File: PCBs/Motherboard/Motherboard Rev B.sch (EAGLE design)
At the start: 29 parts, among them Q1 32kHZ, U1 Value, U2 TPS22942DCKR

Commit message: So. many. changes.
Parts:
- removed U2: TPS22942DCKR, TPS22942:TPS22942DCKR
- added C14: 10uF, adafruit:C-USC0805
- added DF11: DF11-8DP-2DS(52), DF11:DF11-8DP-2DS(52)
- added J1: MOLEX_504050-0491, Molex 504050-0491:MOLEX_504050-0491
- added JTAG_PWR: MOLEX_SL_03-87898, molex-sl-connectors_jw:MOLEX_SL_03-87898
- added LTC6081: LTC6081HMS8PBF, LTC6081:LTC6081HMS8PBF
- added R10, R11, R17, R18, R19, R9: 350, resistor:R-US_R0805
- added R12, R20: 50, Bourns 3224J:3224J
- added R13, R14, R21, R22: 10k, resistor:R-US_R0805
- added R15, R16, R23, R24: 330k, resistor:R-US_R0805
- added R6, R8: 100k, resistor:R-US_R0805
- added R7: 0, resistor:R-US_R0805
- added TPS22942: TPS22942DCKR, TPS22942:TPS22942DCKR
- added U$3: FPF2105, FPF2105:FPF2105
- C12: value 2.2nF -> 1nF
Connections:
- removed net INT: U$2.INT
- removed net N$4 (its old number): C18.1, Q1.1, U1.PJ.7_HFXOUT
- removed net RST: C12.1, JTAG-11.KL, R5.1, U1.RST_NMI_SBWTDIO_N
- removed net TCK: JTAG-7.KL, U1.PJ.3_TCK_SRCPUOFF_C9
- removed net TDI: JTAG-3.KL, U1.PJ.1_TDI_TCLK_MCLK_SRSCG0_C7
- removed net TDO: JTAG-1.KL, U1.PJ.0_TDO_TB0OUTH_SMCLK_SRSCG1_C6
- removed net TEST: JTAG-8.KL, U1.TEST_SBWTCK
- removed net TMS: JTAG-5.KL, U1.PJ.2_TMS_ACLK_SROSCOFF_C8
- new net 3V1: C14.1
- new net 3V3_SD: C13.1, C16.1, R1.1, U$11.VDD, U$3.VOUT
- new net EXT_RXD: JTAG-14.KL, U1.P2.6_TB0.1_UCA1RXD_UCA1SOMI
- new net EXT_TXD: JTAG-12.KL, U1.P2.5_TB0.0_UCA1TXD_UCA1SIMO
- new net INT_IMU: U$2.INT, U1.P8.1
- new net N$10: LTC6081.-INA, R14.2, R16.2
- new net N$11: R18.2, R19.1, R21.1
- new net N$12: LTC6081.+INB, R21.2, R23.2
- new net N$13: LTC6081.-INB, R22.2, R24.2
- new net N$2: R6.2, R7.2, U$3.ON
- new net N$6: C18.1, Q1.1, U1.PJ.4_LFXIN
- new net N$7: R8.2, U$3.FLAGB
- new net N$8: R10.2, R11.1, R13.1
- new net N$9: LTC6081.+INA, R13.2, R15.2
- new net SBWTCK: JTAG-7.KL, U1.TEST_SBWTCK
- new net SBWTDIO: C12.1, JTAG-1.KL, R5.1, U1.RST_NMI_SBWTDIO_N
- new net STR1: LTC6081.OUTA, R16.1, U1.P3.1_A13_C13
- new net STR1_L1: DF11.1, R12.WIPER
- new net STR1_L2: DF11.2, R9.2
- new net STR1_L3: DF11.3, R14.1
- new net STR2: LTC6081.OUTB, R24.1, U1.P3.2_A14_C14
- new net STR2_L1: DF11.4, R20.WIPER
- new net STR2_L2: DF11.5, R17.2
- new net STR2_L3: DF11.6, R22.1
- new net SW5: J1.1, U$1.SW5_5V
- new net TMP_L1: DF11.7
- new net TMP_L2: DF11.8
- new net VCC_TARGET: JTAG-4.KL, JTAG_PWR.3
- new net VCC_TOOL: JTAG-2.KL, JTAG_PWR.1
- net 3V3: now also R8.1, TPS22942.VIN, U$3.VIN; no longer C13.1, C16.1, R1.1, U$11.VDD, U2.VIN
- net 3V3_UC: now also JTAG_PWR.2, TPS22942.VOUT; no longer U2.VOUT
- net CS_SD: now also U1.P4.0_A8; no longer U1.P1.3_TA1.2_UCB0STE_A3_C3
- net GND: now also C14.2, J1.4, J1.SHIELD, LTC6081.V-, R10.1, R15.1, R17.1, R18.1, R23.1, R6.1, R9.1, TPS22942.GND, U$3.GND; no longer U2.GND
- net LI_OA_RESET: now also R7.1
- net N$1: now also TPS22942.OC; no longer U2.OC
- net N$5: now also TPS22942.ON; no longer U2.ON
- net SCL: now also J1.2
- net SDA: now also J1.3
- net SW10: now also LTC6081.V+, R11.2, R12.CCW, R19.2, R20.CCW
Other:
- note added: "Antenna Connector"
- note added: "Cap value depends on xtal we're using"
- note added: "JTAG (SBW) Interface"
- note added: "MSP430 Load Switch"
- note added: "SD Load Switch"
- note added: "Sensing"
- note added: "Strain Gauge"
- note removed: "JTAG Interface"
- note removed: "Need to add a jumper on pins 2 & 4 to control power flow!"
- moved on the sheet: C13, C15, C16, C17, C18, C2, C3, C4, JTAG-1, JTAG-10, JTAG-11, JTAG-12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

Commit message: Split I2C and SPI buses
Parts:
- removed DF11: DF11-8DP-2DS(52), DF11:DF11-8DP-2DS(52)
- removed J1: MOLEX_504050-0491, Molex 504050-0491:MOLEX_504050-0491
- removed JTAG: 2514-5, con-3m:2514-5
- removed LTC6081: LTC6081HMS8PBF, LTC6081:LTC6081HMS8PBF
- removed R15, R16, R23, R24: 330k, resistor:R-US_R0805
- removed R17, R18, R19: 350, resistor:R-US_R0805
- removed R20: 50, Bourns 3224J:3224J
- removed R21, R22: 10k, resistor:R-US_R0805
- added AD8228: AD8228BRZ, AD8228:AD8228BRZ
- added C19, C20, C21, C22, C23: 0.1uF, resistor:C-USC0805
- added J2: MOLEX_504050-0491, Molex 504050-0491:MOLEX_504050-0491
- added REF3330: REF3330_DBZ_3, REF3330:REF3330_DBZ_3
- added TLV2461-1, TLV2461-2, TLV2461-3: TLV2461A_D_8, TLV2461:TLV2461A_D_8
- added X1: 2514-5, con-3m:2514-5
- C17, C18: value 10pF -> 6pF
- R10, R11: value 350 -> 10k
- R12: value 50 -> 100; device Bourns 3224J:3224J -> resistor:R-US_R0805
- R13, R14: value 10k -> 0
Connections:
- removed net MISO: U$11.DATA_OUT, U$2.ADO/SDO, U1.P1.7_TB0.4_UCB0SOMI_UCB0SCL_TA1.0
- removed net MOSI: U$11.DATA_IN, U$2.SDA/SDI, U1.P1.6_TB0.3_UCB0SIMO_UCB0SDA_TA0.0
- removed net N$12: LTC6081.+INB, R21.2, R23.2
- removed net N$13: LTC6081.-INB, R22.2, R24.2
- removed net SCL: J1.2, U$1.I2C_CLK, U1.P7.1_UCB2SOMI_UCB2SCL
- removed net SCLK: U$11.SCLK, U$2.SCL/SCLK, U1.P2.2_TB0.2_UCB0CLK
- removed net SDA: J1.3, U$1.I2C_DATA, U1.P7.0_UCB2SIMO_UCB2SDA
- removed net STR1: LTC6081.OUTA, R16.1, U1.P3.1_A13_C13
- removed net STR1_L1: DF11.1, R12.WIPER
- removed net STR1_L2: DF11.2, R9.2
- removed net STR1_L3: DF11.3, R14.1
- removed net STR2: LTC6081.OUTB, R24.1, U1.P3.2_A14_C14
- removed net STR2_L1: DF11.4, R20.WIPER
- removed net STR2_L2: DF11.5, R17.2
- removed net STR2_L3: DF11.6, R22.1
- removed net TMP_L1: DF11.7
- removed net TMP_L2: DF11.8
- new net 3V: J2.1, J2.3, R11.2, TLV2461-1.IN-, TLV2461-1.OUT
- new net 3V_REF: REF3330.OUT, TLV2461-1.IN+
- new net CLK_IMU: U$2.SCL/SCLK, U1.P5.2_UCB1CLK_TA4CLK
- new net CLK_SD: U$11.SCLK, U1.P2.2_TB0.2_UCB0CLK
- new net JTAG_RXD: R13.1, U1.P2.5_TB0.0_UCA1TXD_UCA1SIMO
- new net JTAG_TXD: R14.1, U1.P2.6_TB0.1_UCA1RXD_UCA1SOMI
- new net MISO_IMU: U$2.ADO/SDO, U1.P5.1_UCB1SOMI_UCB1SCL
- new net MISO_SD: U$11.DATA_OUT, U1.P1.7_TB0.4_UCB0SOMI_UCB0SCL_TA1.0
- new net MOSI_IMU: U$2.SDA/SDI, U1.P5.0_UCB1SIMO_UCB1SDA
- new net MOSI_SD: U$11.DATA_IN, U1.P1.6_TB0.3_UCB0SIMO_UCB0SDA_TA0.0
- new net SCL_ANT: U$1.SCL_ANT, U1.P6.5_UCB3SOMI_UCB3SCL
- new net SCL_EPS: U$1.I2C_CLK, U1.P7.1_UCB2SOMI_UCB2SCL
- new net SDA_ANT: U$1.SDA_ANT, U1.P6.4_UCB3SIMO_UCB3SDA
- new net SDA_EPS: U$1.I2C_DATA, U1.P7.0_UCB2SIMO_UCB2SDA
- new net STRAIN_OUT: AD8228.IN-, AD8228.VOUT, R10.2, R11.1, TLV2461-2.IN+, U1.P3.1_A13_C13
- new net STRN: AD8228.IN+, J2.4, R9.2
- new net TEMP: J2.2, R12.2, TLV2461-3.IN+
- new net TEMP_OUT: TLV2461-3.IN-, TLV2461-3.OUT, U1.P3.2_A14_C14
- net 3V3: now also AD8228.VS+, C21.1
- net EXT_RXD: now also U1.P6.0_UCA3TXD_UCA3SIMO; no longer JTAG-14.KL, U1.P2.6_TB0.1_UCA1RXD_UCA1SOMI
- net EXT_TXD: now also U1.P6.1_UCA3RXD_UCA3SOMI; no longer JTAG-12.KL, U1.P2.5_TB0.0_UCA1TXD_UCA1SIMO
- net GND: now also AD8228.VS-, C19.2, C20.2, C21.2, C22.2, C23.2, R12.1, REF3330.GND, TLV2461-1.GND, TLV2461-2.GND, X1.9; no longer J1.4, J1.SHIELD, JTAG-9.KL, LTC6081.V-, R15.1, R17.1, R18.1, R23.1
- net LITHIUM_RX: now also U1.P5.4_UCA2TXD_UCA2SIMO_TB0OUTH; no longer U1.P5.5_UCA2RXD_UCA2SOMI_ACLK
- net LITHIUM_TX: now also U1.P5.5_UCA2RXD_UCA2SOMI_ACLK; no longer U1.P5.4_UCA2TXD_UCA2SIMO_TB0OUTH
- net N$10: now also TLV2461-3.GND; no longer LTC6081.-INA, R14.2, R16.2
- net N$11: now also R13.2, X1.12; no longer R18.2, R19.1, R21.1
- net N$8: now also R14.2, X1.14; no longer R10.2, R11.1, R13.1
- net N$9: now also AD8228.REF, TLV2461-2.IN-, TLV2461-2.OUT; no longer LTC6081.+INA, R13.2, R15.2
- net PINAVL1_RX: now also U1.P2.0_TB0.6_UCA0TXD_UCA0SIMO_TB0CLK_ACLK; no longer U1.P2.1_TB0.0_UCA0RXD_UCA0SOMI
- net PINAVL1_TX: now also U1.P2.1_TB0.0_UCA0RXD_UCA0SOMI; no longer U1.P2.0_TB0.6_UCA0TXD_UCA0SIMO_TB0CLK_ACLK
- net SBWTCK: now also X1.7; no longer JTAG-7.KL
- net SBWTDIO: now also X1.1; no longer JTAG-1.KL
- net SW10: now also C19.1, C20.1, C22.1, C23.1, REF3330.IN, TLV2461-1.VDD+, TLV2461-2.VDD+, TLV2461-3.VDD+; no longer LTC6081.V+, R11.2, R12.CCW, R19.2, R20.CCW
- net SW5: no longer J1.1
- net VCC_TARGET: now also X1.4; no longer JTAG-4.KL
- net VCC_TOOL: now also X1.2; no longer JTAG-2.KL
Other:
- note added: "Add external UART pins"
- note added: "Av=10"
- note added: "Need card detect"
- note added: "Sensing harness"
- note added: "Temperature"
- note added: "Voltage Reference"
- note removed: "Antenna Connector"
- note removed: "Sensing"
- moved on the sheet: C13, C14, C16, JTAG_PWR, R1, R10, R11, R13, R14, R2, R6, R7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

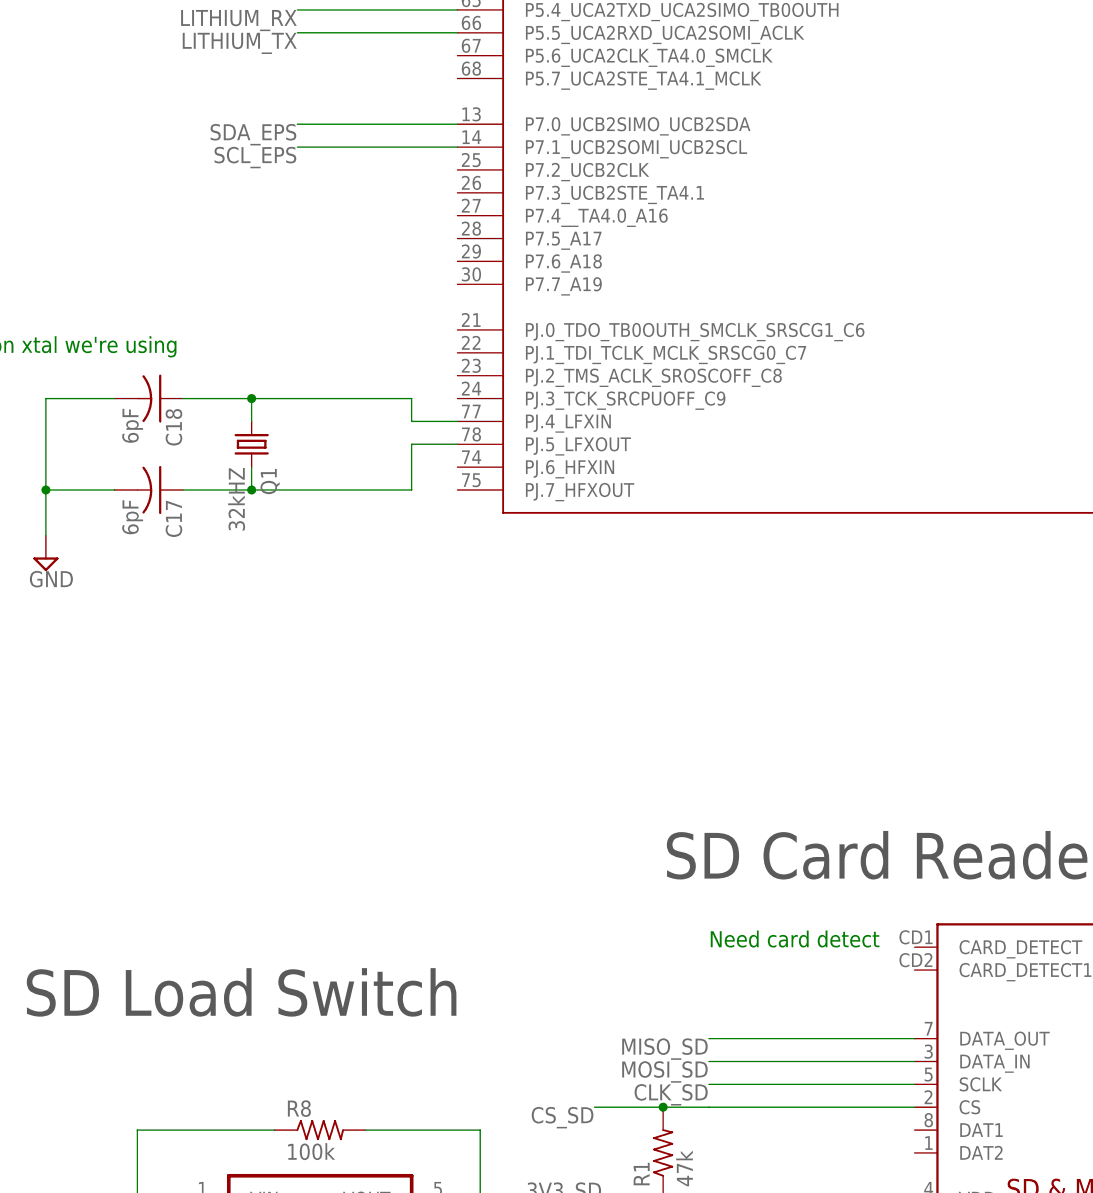
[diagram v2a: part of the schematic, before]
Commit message: Add SD card detect to 7.2
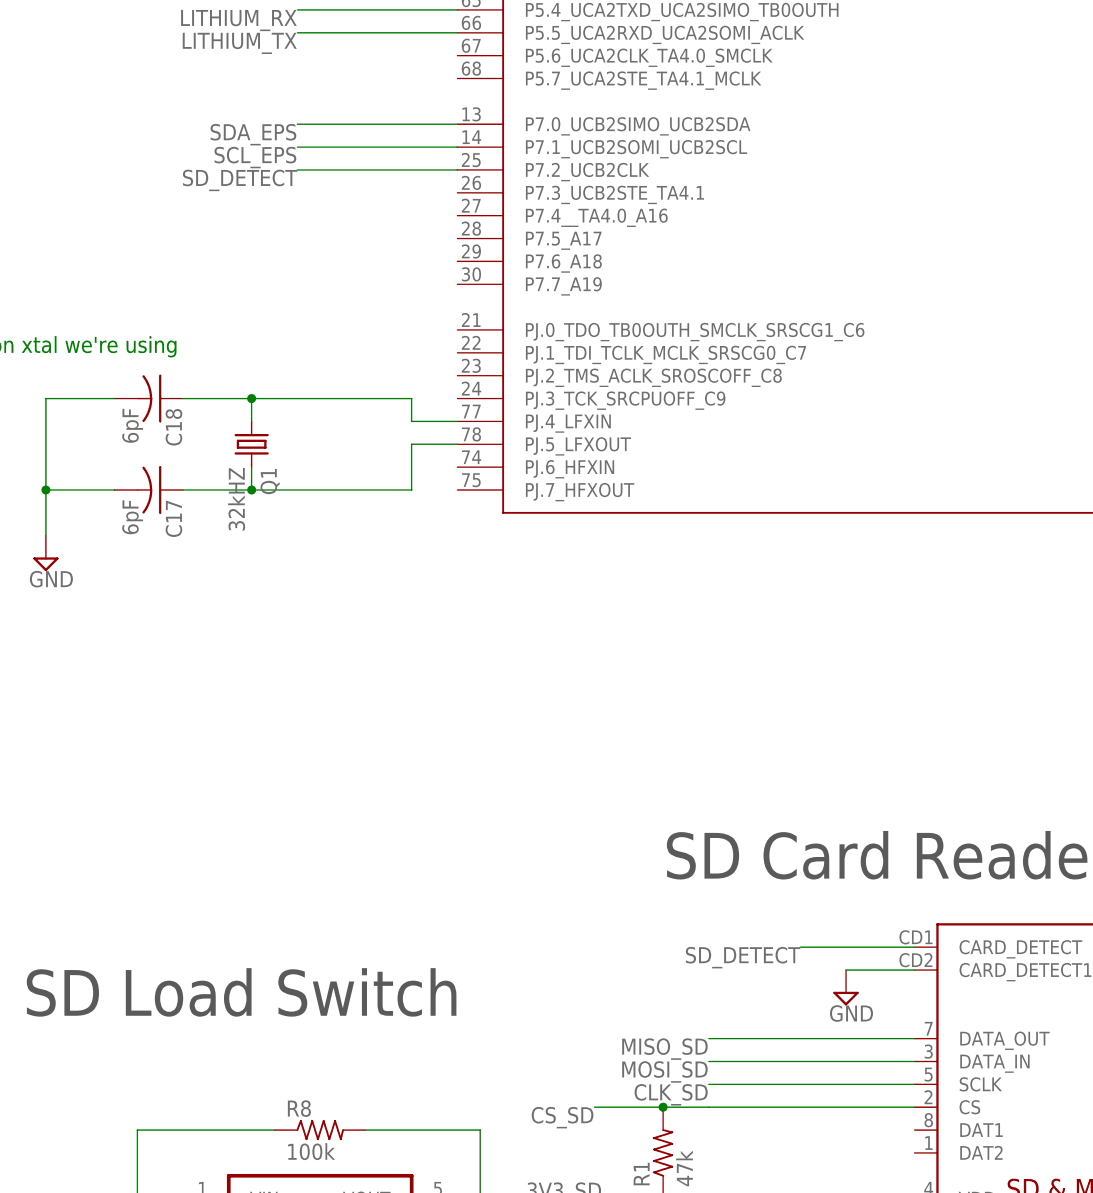
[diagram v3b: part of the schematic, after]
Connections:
- new net SD_DETECT: U$11.CARD_DETECT, U1.P7.2_UCB2CLK
- net GND: now also U$11.CARD_DETECT1
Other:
- note removed: "Need card detect"
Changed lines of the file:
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@@
 <part name="R13" library="resistor" library_urn="urn:adsk.eagle:library:348" deviceset="R-US_" device="R0805" package3d_urn="urn:adsk.eagle:package:23553/2" value="0"/>
 <part name="R14" library="resistor" library_urn="urn:adsk.eagle:library:348" deviceset="R-US_" device="R0805" package3d_urn="urn:adsk.eagle:package:23553/2" value="0"/>
+<part name="SUPPLY36" library="supply2" library_urn="urn:adsk.eagle:library:372" deviceset="GND" device=""/>
 </parts>
 <sheets>
@@
 <text x="731.52" y="93.98" size="1.778" layer="91">Add external UART pins</text>
 <text x="231.14" y="-78.74" size="1.778" layer="91">Av=10</text>
-<text x="553.72" y="-38.1" size="1.778" layer="91">Need card detect</text>
 </plain>
 <instances>
@@
 <instance part="R13" gate="G$1" x="365.76" y="30.48" rot="R90"/>
 <instance part="R14" gate="G$1" x="358.14" y="30.48" rot="R90"/>
+<instance part="SUPPLY36" gate="GND" x="568.96" y="-43.18"/>
 </instances>
 <busses>
@@
 <wire x1="401.32" y1="-50.8" x2="401.32" y2="-53.34" width="0.1524" layer="91"/>
 <pinref part="SUPPLY35" gate="GND" pin="GND"/>
+</segment>
+<segment>
+<pinref part="U$11" gate="G$1" pin="CARD_DETECT1"/>
+<wire x1="576.58" y1="-40.64" x2="568.96" y2="-40.64" width="0.1524" layer="91"/>
+<pinref part="SUPPLY36" gate="GND" pin="GND"/>
 </segment>
 </net>
@@
 </segment>
 </net>
+<net name="SD_DETECT" class="0">
+<segment>
+<pinref part="U$11" gate="G$1" pin="CARD_DETECT"/>
+<wire x1="576.58" y1="-38.1" x2="563.88" y2="-38.1" width="0.1524" layer="91"/>
+<label x="563.88" y="-38.1" size="1.778" layer="95" rot="R180"/>
+</segment>
+<segment>
+<pinref part="U1" gate="A" pin="P7.2_UCB2CLK"/>
+<wire x1="525.78" y1="48.26" x2="508" y2="48.26" width="0.1524" layer="91"/>
+<label x="508" y="48.26" size="1.778" layer="95" rot="R180"/>
+</segment>
+</net>

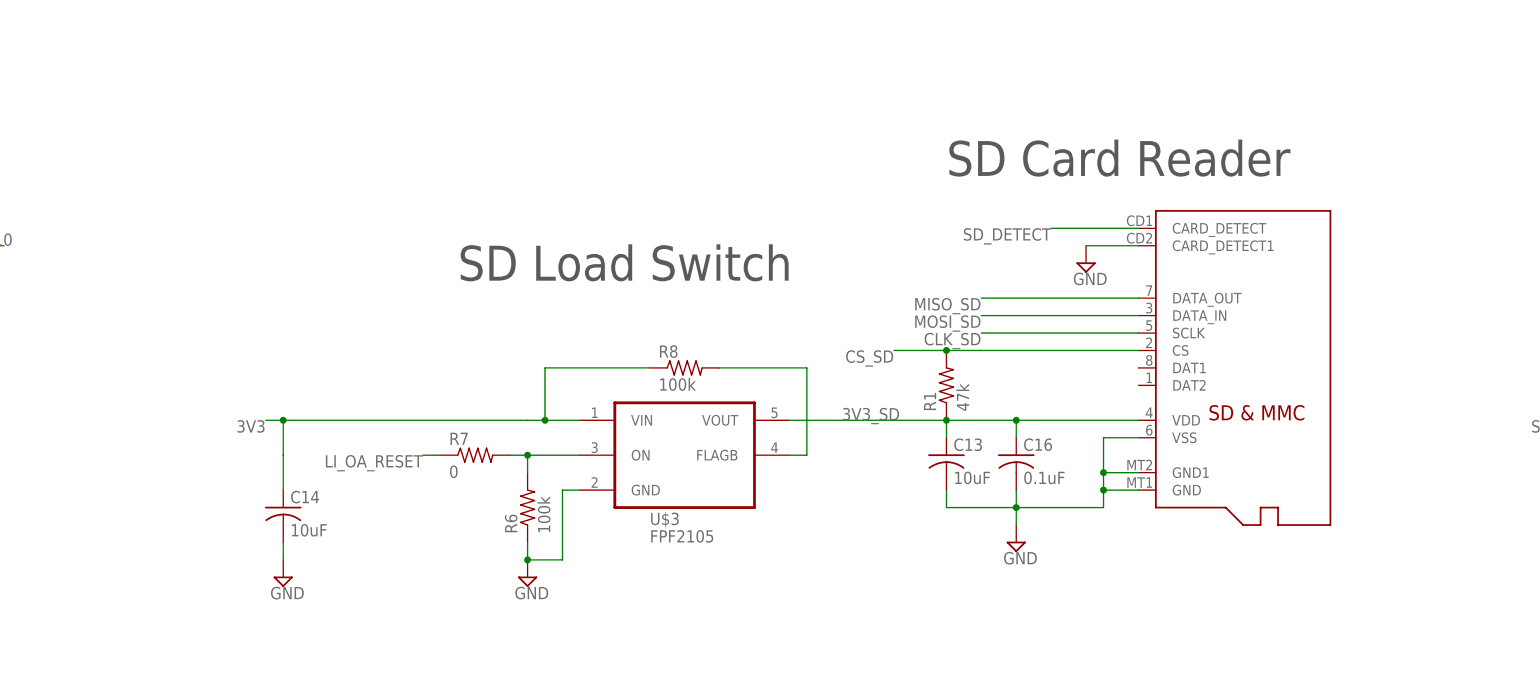
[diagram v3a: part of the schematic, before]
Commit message: Replace SD connector with a model hand-solderable
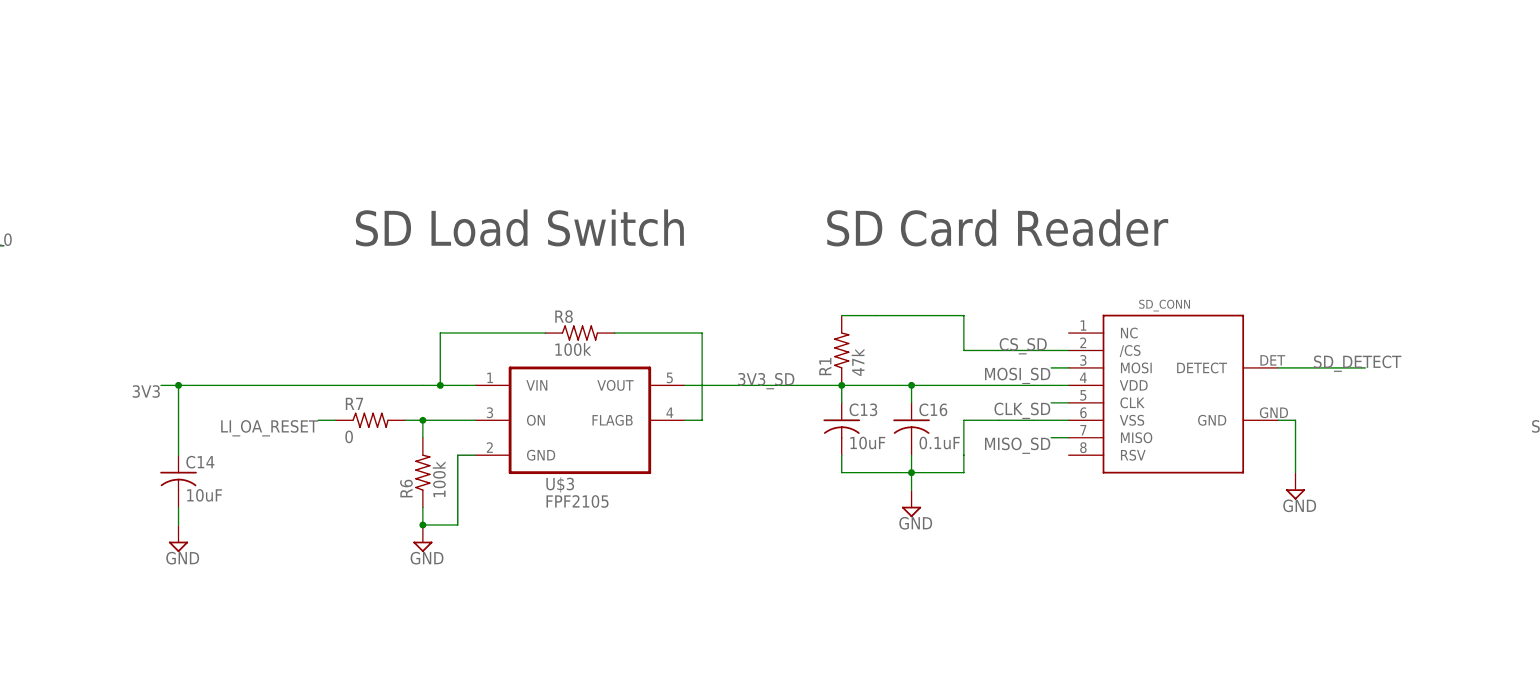
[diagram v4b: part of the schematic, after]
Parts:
- removed U$11: MICROSD, adafruit:MICROSD
- added SD_CONN: 502702-0891, Molex SD - 502702:502702-0891
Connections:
- net 3V3_SD: now also SD_CONN.VDD; no longer U$11.VDD
- net CLK_SD: now also SD_CONN.CLK; no longer U$11.SCLK
- net CS_SD: now also SD_CONN./CS; no longer U$11.CS
- net GND: now also SD_CONN.GND, SD_CONN.VSS; no longer U$11.CARD_DETECT1, U$11.GND, U$11.GND1, U$11.VSS
- net MISO_SD: now also SD_CONN.MISO; no longer U$11.DATA_OUT
- net MOSI_SD: now also SD_CONN.MOSI; no longer U$11.DATA_IN
- net SD_DETECT: now also SD_CONN.DETECT; no longer U$11.CARD_DETECT
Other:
- moved on the sheet: C13, C14, C16, R1, R6, R7, R8, U$3
